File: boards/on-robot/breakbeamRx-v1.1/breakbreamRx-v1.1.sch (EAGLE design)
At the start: 4 parts, among them J1 0436500213

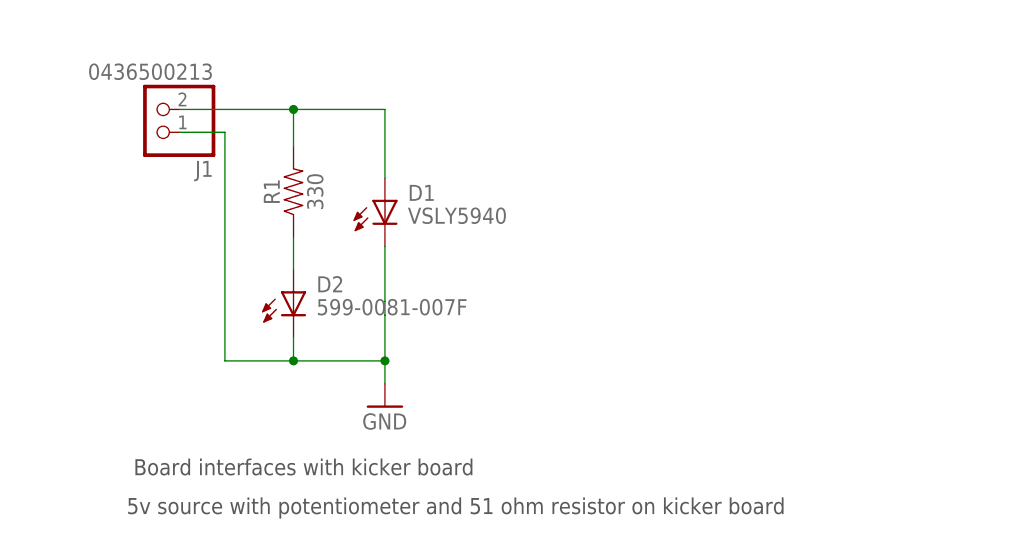
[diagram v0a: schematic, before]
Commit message: Fixed Breakbeam RX width and reverted back to old TX (#66)
* Fixed Breakbeam RX width and reverted back to old TX

* Removed bbtx-v1.0 from archive

---------

Co-authored-by: Emm <emmcchesney@mcdonogh.org>
Co-authored-by: bperez40 <bperez40@gatech.edu>
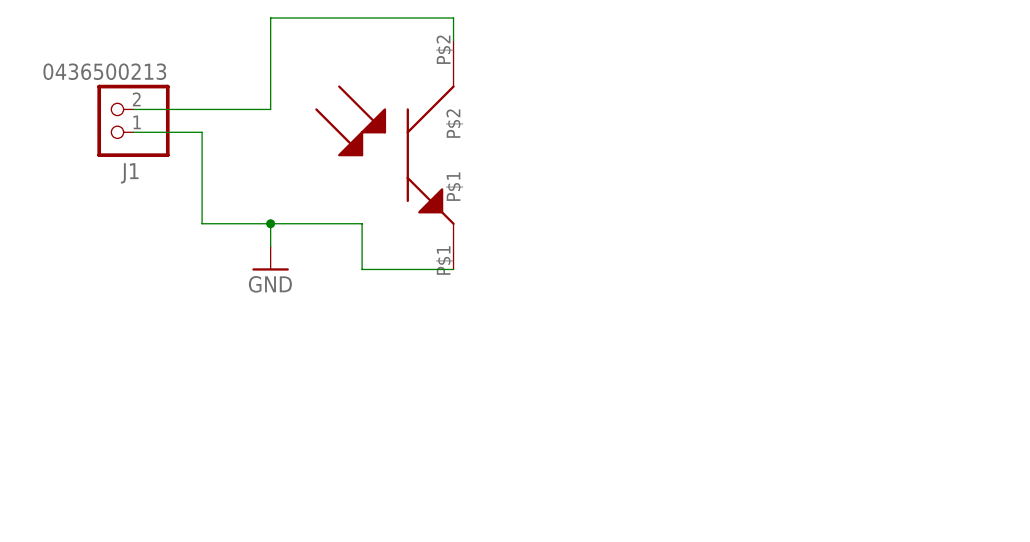
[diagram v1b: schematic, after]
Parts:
- removed D1: VSLY5940, RoboJackets-LEDs:VSLY5940
- removed D2: 599-0081-007F, RoboJackets-LEDs:599-0081-007F
- removed R1: 330, RoboJackets-Resistors:R330-0603-1/10W-5%
- added Q1: LTR-209, RoboJackets-Discrete:LTR-209
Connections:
- removed net BB_TX: D1.A, J1.2, R1.2
- removed net N$2: D2.A, R1.1
- new net RX: J1.2, Q1.P$2
- net GND: now also Q1.P$1; no longer D1.K, D2.K
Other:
- note removed: "5v source with potentiometer and 51 ohm resistor on kicker board"
- note removed: "Board interfaces with kicker board"
- moved on the sheet: J1
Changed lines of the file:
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@@
 <parts>
 <part name="FRAME1" library="RoboJackets-Frames" deviceset="FRAME_11_17" device="">
-<attribute name="SCH_DESC" value="Breakbeam transceiver board"/>
+<attribute name="SCH_DESC" value="Breakbeam receiver board"/>
 <attribute name="TEAM" value="RoboCup"/>
 </part>
+<part name="J1" library="RoboJackets-Connectors" deviceset="0436500213" device="" override_package3d_urn="urn:adsk.eagle:package:33302042/2" override_package_urn="urn:adsk.eagle:footprint:33302043/1" override_locally_modified="yes"/>
 <part name="SUPPLY1" library="RoboJackets-Supplies" deviceset="GND" device=""/>
-<part name="J1" library="RoboJackets-Connectors" deviceset="0436500213" device="" override_package3d_urn="urn:adsk.eagle:package:33521981/2" override_package_urn="urn:adsk.eagle:footprint:33521982/1"/>
-<part name="R1" library="RoboJackets-Resistors" deviceset="R330" device="-0603-1/10W-5%" package3d_urn="urn:adsk.eagle:package:39650/1" value="330"/>
-<part name="D1" library="RoboJackets-LEDs" deviceset="VSLY5940" device=""/>
-<part name="D2" library="RoboJackets-LEDs" deviceset="599-0081-007F" device=""/>
+<part name="Q1" library="RoboJackets-Discrete" deviceset="LTR-209" device=""/>
 </parts>
 <sheets>
 <sheet>
 <plain>
-<text x="0" y="-38.1" size="1.778" layer="97">Board interfaces with kicker board</text>
-<text x="-0.762" y="-42.418" size="1.778" layer="97">5v source with potentiometer and 51 ohm resistor on kicker board</text>
 </plain>
 <instances>
-<instance part="FRAME1" gate="G$1" x="-182.88" y="-121.92" smashed="yes"/>
-<instance part="FRAME1" gate="G$2" x="142.24" y="-121.92" smashed="yes">
-<attribute name="LAST_DATE_TIME" x="154.94" y="-120.65" size="2.54" layer="94"/>
-<attribute name="SHEET" x="228.6" y="-120.65" size="2.54" layer="94"/>
-<attribute name="DRAWING_NAME" x="157.48" y="-102.87" size="2.54" layer="94"/>
-<attribute name="TEAM" x="144.018" y="-90.678" size="3.81" layer="94" ratio="10" align="top-left"/>
-<attribute name="REVISION" x="214.63" y="-115.57" size="2.54" layer="94"/>
-<attribute name="SCH_DESC" x="143.51" y="-115.57" size="2.54" layer="94"/>
+<instance part="FRAME1" gate="G$1" x="-184" y="-148" smashed="yes"/>
+<instance part="FRAME1" gate="G$2" x="141.12" y="-148" smashed="yes">
+<attribute name="LAST_DATE_TIME" x="153.82" y="-146.73" size="2.54" layer="94"/>
+<attribute name="SHEET" x="227.48" y="-146.73" size="2.54" layer="94"/>
+<attribute name="DRAWING_NAME" x="156.36" y="-128.95" size="2.54" layer="94"/>
+<attribute name="TEAM" x="142.898" y="-116.25" size="3.81" layer="94" ratio="10" align="top-left"/>
+<attribute name="REVISION" x="213.51" y="-141.65" size="2.54" layer="94"/>
+<attribute name="SCH_DESC" x="142.39" y="-141.65" size="2.54" layer="94"/>
 </instance>
-<instance part="SUPPLY1" gate="G$1" x="27.94" y="-30.48" smashed="yes">
-<attribute name="VALUE" x="25.4" y="-33.02" size="1.778" layer="96"/>
+<instance part="J1" gate="G$1" x="-2.54" y="2.54" smashed="yes" rot="R180">
+<attribute name="NAME" x="0.762" y="-3.429" size="1.778" layer="95" rot="R180"/>
+<attribute name="VALUE" x="3.81" y="7.62" size="1.778" layer="96" rot="R180"/>
 </instance>
-<instance part="J1" gate="G$1" x="2.54" y="2.54" smashed="yes" rot="R180">
-<attribute name="NAME" x="8.89" y="-3.175" size="1.778" layer="95" rot="R180"/>
-<attribute name="VALUE" x="8.89" y="7.62" size="1.778" layer="96" rot="R180"/>
+<instance part="SUPPLY1" gate="G$1" x="15.24" y="-15.24" smashed="yes">
+<attribute name="VALUE" x="12.7" y="-17.78" size="1.778" layer="96"/>
 </instance>
-<instance part="R1" gate="A" x="17.78" y="-6.604" smashed="yes" rot="R90">
-<attribute name="NAME" x="16.256" y="-6.604" size="1.778" layer="95" font="vector" rot="R90" align="bottom-center"/>
-<attribute name="VALUE" x="19.304" y="-6.604" size="1.778" layer="96" font="vector" rot="R90" align="top-center"/>
-</instance>
-<instance part="D1" gate="G$1" x="27.94" y="-10.16" smashed="yes">
-<attribute name="NAME" x="30.48" y="-7.62" size="1.778" layer="95"/>
-<attribute name="VALUE" x="30.48" y="-10.16" size="1.778" layer="96"/>
-</instance>
-<instance part="D2" gate="A" x="17.78" y="-20.32" smashed="yes">
-<attribute name="NAME" x="20.32" y="-17.78" size="1.778" layer="95"/>
-<attribute name="VALUE" x="20.32" y="-20.32" size="1.778" layer="96"/>
-</instance>
+<instance part="Q1" gate="G$1" x="30.48" y="-2.54" smashed="yes"/>
 </instances>
 <busses>
 </busses>
 <nets>
+<net name="RX" class="0">
+<segment>
+<pinref part="J1" gate="G$1" pin="2"/>
+<wire x1="15.24" y1="2.54" x2="0" y2="2.54" width="0.1524" layer="91"/>
+<wire x1="15.24" y1="2.54" x2="15.24" y2="12.7" width="0.1524" layer="91"/>
+<wire x1="15.24" y1="12.7" x2="35.56" y2="12.7" width="0.1524" layer="91"/>
+<pinref part="Q1" gate="G$1" pin="P$2"/>
+<wire x1="35.56" y1="12.7" x2="35.56" y2="10.16" width="0.1524" layer="91"/>
+</segment>
+</net>
 <net name="GND" class="0">
 <segment>
+<wire x1="7.62" y1="-10.16" x2="7.62" y2="0" width="0.1524" layer="91"/>
+<pinref part="J1" gate="G$1" pin="1"/>
+<wire x1="7.62" y1="0" x2="0" y2="0" width="0.1524" layer="91"/>
 <pinref part="SUPPLY1" gate="G$1" pin="GND"/>
-<wire x1="27.94" y1="-25.4" x2="27.94" y2="-27.94" width="0.1524" layer="91"/>
-<wire x1="27.94" y1="-25.4" x2="17.78" y2="-25.4" width="0.1524" layer="91"/>
-<wire x1="17.78" y1="-25.4" x2="10.16" y2="-25.4" width="0.1524" layer="91"/>
-<wire x1="17.78" y1="-22.86" x2="17.78" y2="-25.4" width="0.1524" layer="91"/>
-<junction x="17.78" y="-25.4"/>
-<pinref part="J1" gate="G$1" pin="1"/>
-<wire x1="5.08" y1="0" x2="10.16" y2="0" width="0.1524" layer="91"/>
-<wire x1="10.16" y1="0" x2="10.16" y2="-25.4" width="0.1524" layer="91"/>
-<wire x1="27.94" y1="-25.4" x2="27.94" y2="-20.32" width="0.1524" layer="91"/>
-<junction x="27.94" y="-25.4"/>
-<pinref part="D1" gate="G$1" pin="K"/>
-<wire x1="27.94" y1="-20.32" x2="27.94" y2="-18.796" width="0.1524" layer="91"/>
-<wire x1="27.94" y1="-12.7" x2="27.94" y2="-18.796" width="0.1524" layer="91"/>
-<pinref part="D2" gate="A" pin="K"/>
-</segment>
-</net>
-<net name="BB_TX" class="0">
-<segment>
-<pinref part="J1" gate="G$1" pin="2"/>
-<wire x1="5.08" y1="2.54" x2="17.78" y2="2.54" width="0.1524" layer="91"/>
-<wire x1="17.78" y1="2.54" x2="27.94" y2="2.54" width="0.1524" layer="91"/>
-<junction x="17.78" y="2.54"/>
-<pinref part="R1" gate="A" pin="2"/>
-<wire x1="17.78" y1="-1.524" x2="17.78" y2="2.54" width="0.1524" layer="91"/>
-<pinref part="D1" gate="G$1" pin="A"/>
-<wire x1="27.94" y1="2.54" x2="27.94" y2="-5.08" width="0.1524" layer="91"/>
-</segment>
-</net>
-<net name="N$2" class="0">
-<segment>
-<pinref part="R1" gate="A" pin="1"/>
-<wire x1="17.78" y1="-15.24" x2="17.78" y2="-11.684" width="0.1524" layer="91"/>
-<pinref part="D2" gate="A" pin="A"/>
+<wire x1="7.62" y1="-10.16" x2="15.24" y2="-10.16" width="0.1524" layer="91"/>
+<wire x1="15.24" y1="-10.16" x2="15.24" y2="-12.7" width="0.1524" layer="91"/>
+<wire x1="15.24" y1="-10.16" x2="25.4" y2="-10.16" width="0.1524" layer="91"/>
+<wire x1="25.4" y1="-10.16" x2="25.4" y2="-15.24" width="0.1524" layer="91"/>
+<junction x="15.24" y="-10.16"/>
+<pinref part="Q1" gate="G$1" pin="P$1"/>
+<wire x1="25.4" y1="-15.24" x2="35.56" y2="-15.24" width="0.1524" layer="91"/>
 </segment>
 </net>
@@
 <compatibility>
 <note version="8.3" severity="warning">
-Since Version 8.3, EAGLE supports URNs for individual library
-assets (packages, symbols, and devices). The URNs of those assets
-will not be understood (or retained) with this version.
-</note>
-<note version="8.3" severity="warning">
 Since Version 8.3, EAGLE supports the association of 3D packages
